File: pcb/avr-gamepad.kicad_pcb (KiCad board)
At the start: 2 copper layers, 53.1 x 53 mm, 56 parts, among them J1 Conn_01x06, J2 Conn_01x06, J3 Conn_01x05, J4 Conn_01x05, P1 USB_C_Plug_USB2.0, SW1 RESET, SW10 R2, SW11 A, SW13 Left, SW14 L2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

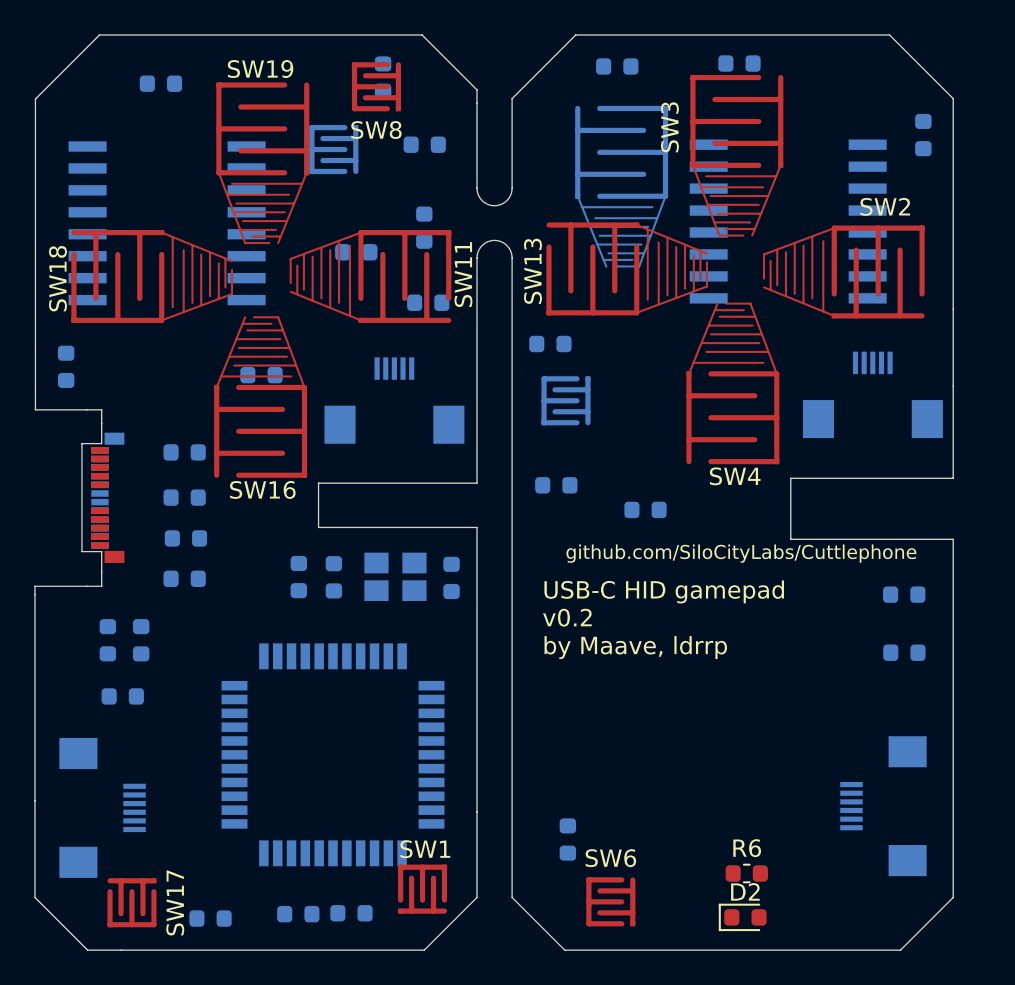
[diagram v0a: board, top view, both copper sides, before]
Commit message: change triggers to tact switches, add footprint
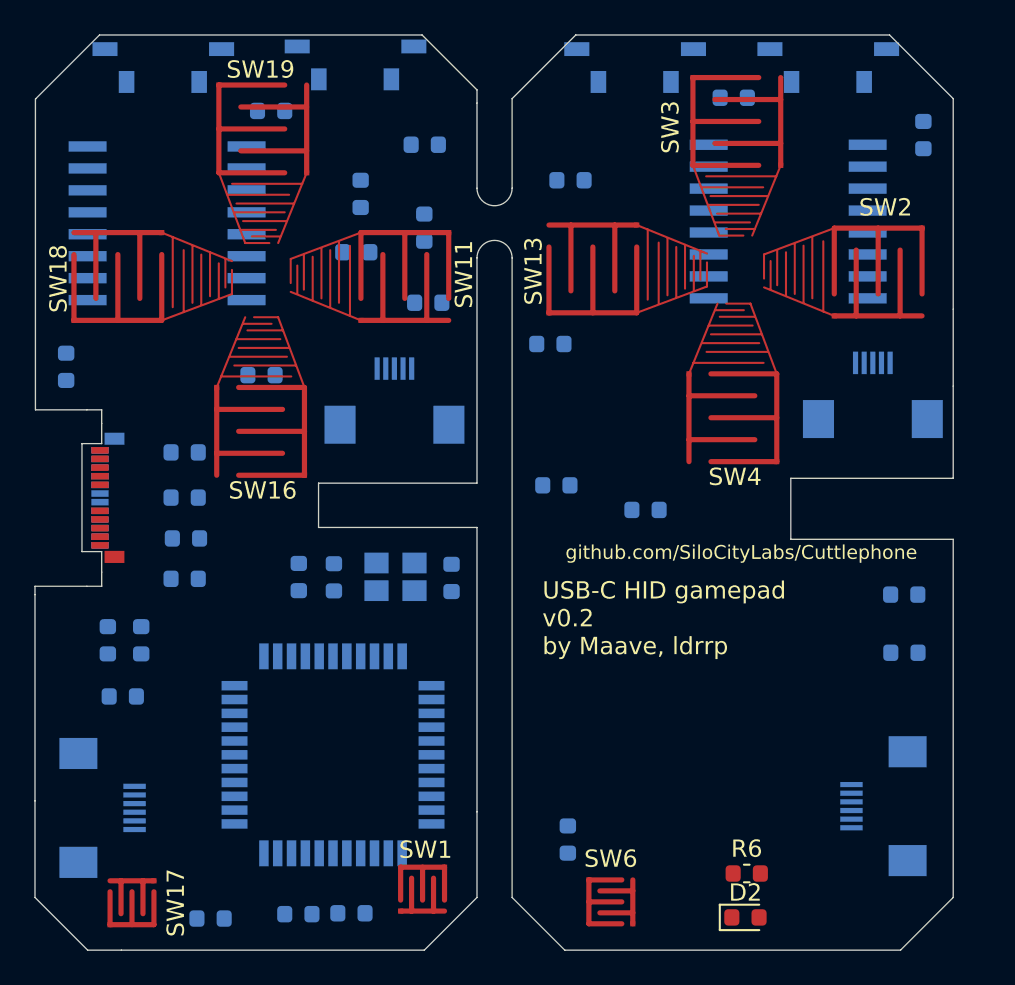
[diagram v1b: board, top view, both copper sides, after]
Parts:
- SW10, SW14: footprint button-contacts:Small -> right-angle-tact:TL3330
- SW7: footprint button-contacts:Large_tapered -> right-angle-tact:TL3330
- SW8: footprint button-contacts:Small -> right-angle-tact:TL3330; moved to B.Cu
- moved SW14 24.6 mm to (173.3, 82.2)
- moved SW10 11.0 mm to (134.9, 82.2)
- moved D4 7.12 mm to (158.4, 88.8), turned to 180 degrees
- moved D12 6.85 mm to (146.3, 89.6)
- moved D17 6.57 mm to (141.1, 84.8)
- moved SW7 5.03 mm to (162.2, 82.2), turned to 0 degrees
- moved D8 2.01 mm to (167.9, 84.0)
- moved SW8 1.82 mm to (146.0, 82.1)

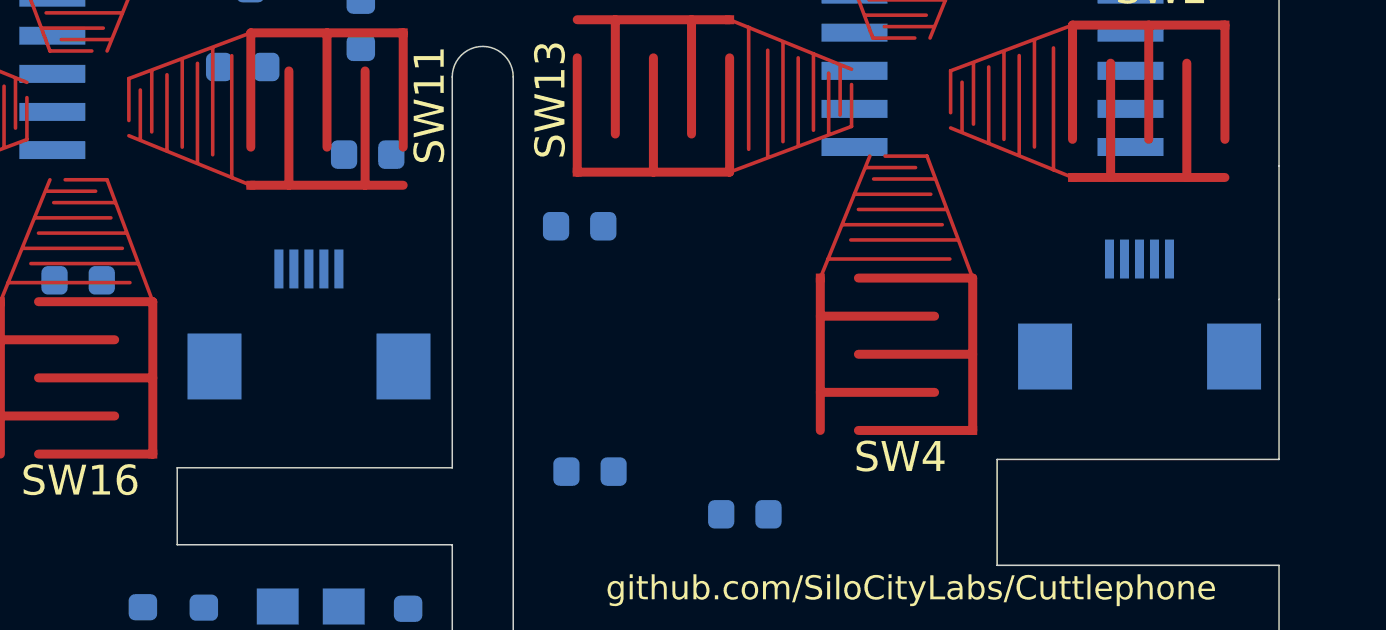
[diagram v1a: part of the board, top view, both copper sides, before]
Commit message: change 5-pin ffc to molex
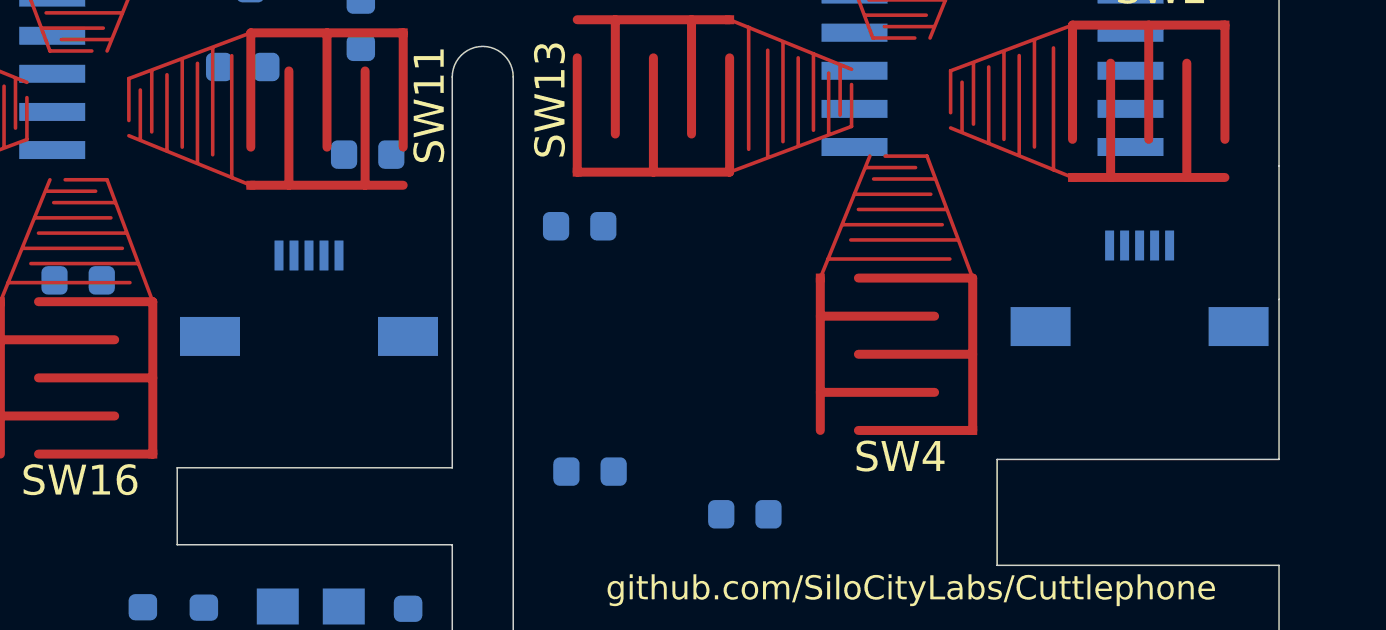
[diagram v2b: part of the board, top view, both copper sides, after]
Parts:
- J3, J4: footprint uxcell-ffc:uxcell_ffc_0.5pitch_1x05 -> molex_5051100592:5051100592

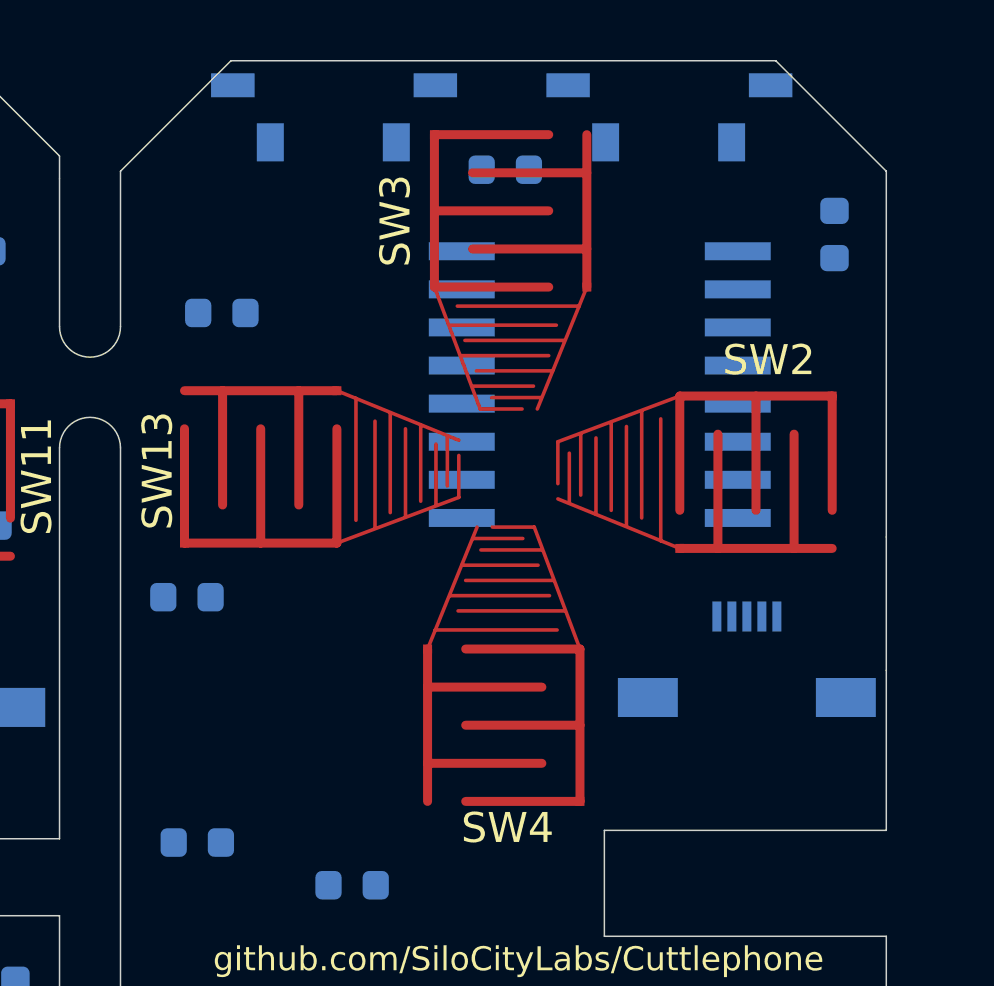
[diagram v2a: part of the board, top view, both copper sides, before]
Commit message: improve d-pad contacts
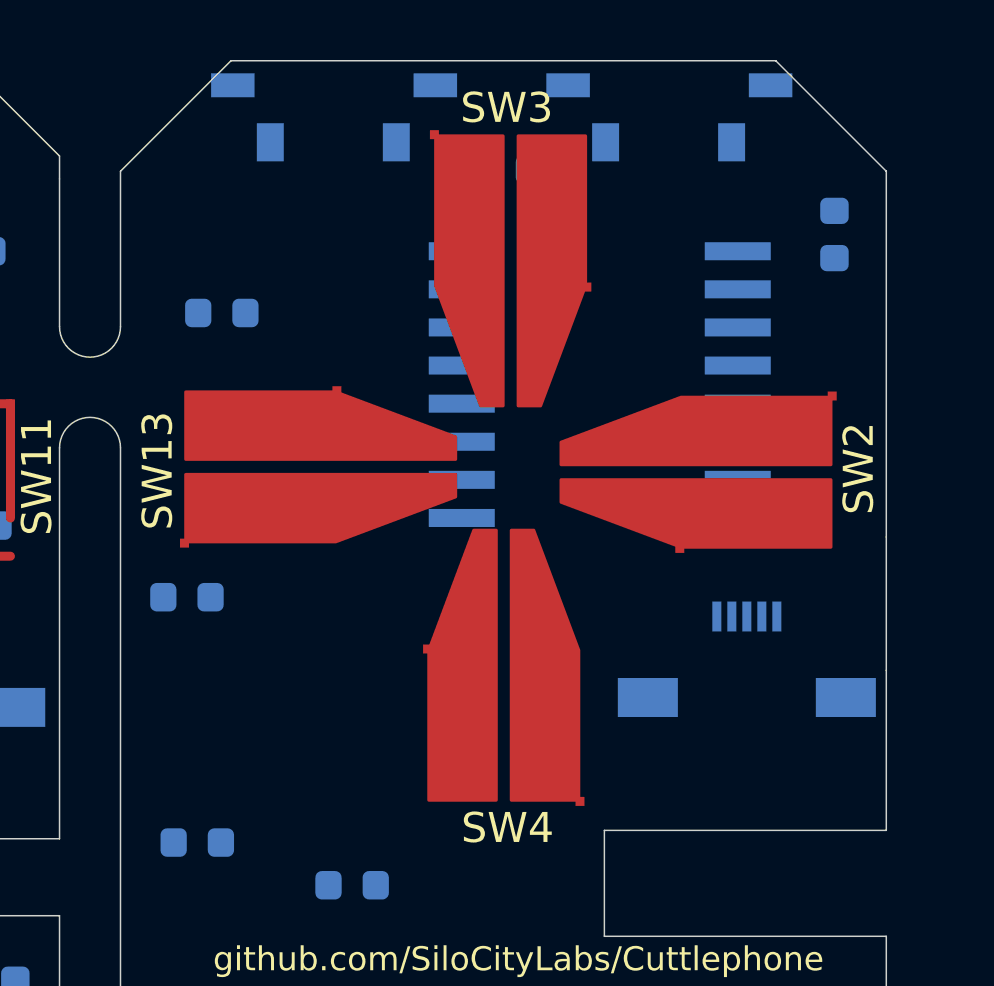
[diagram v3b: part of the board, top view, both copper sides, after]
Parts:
- SW13, SW2, SW3, SW4: footprint button-contacts:Large_tapered -> button-contacts:Dpad_Large_tapered

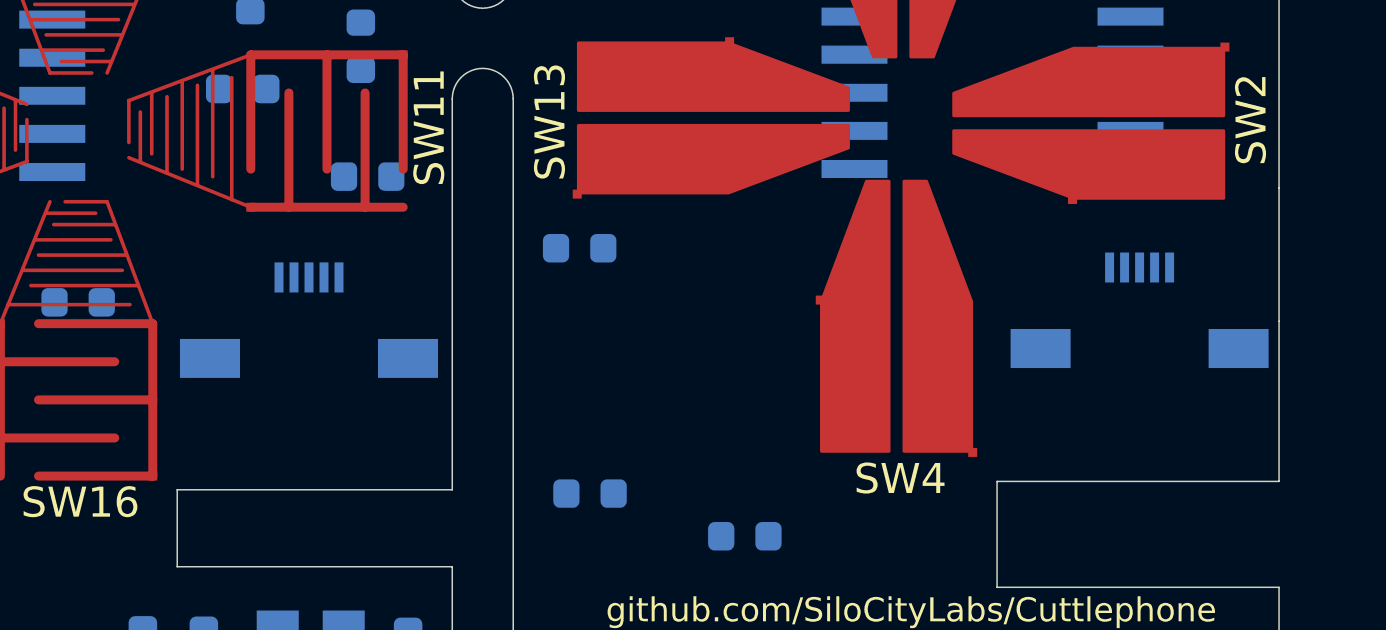
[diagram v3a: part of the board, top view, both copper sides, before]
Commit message: fix geometry calculations with BOSL shapes, add 1x04 FFC, experimental trigger
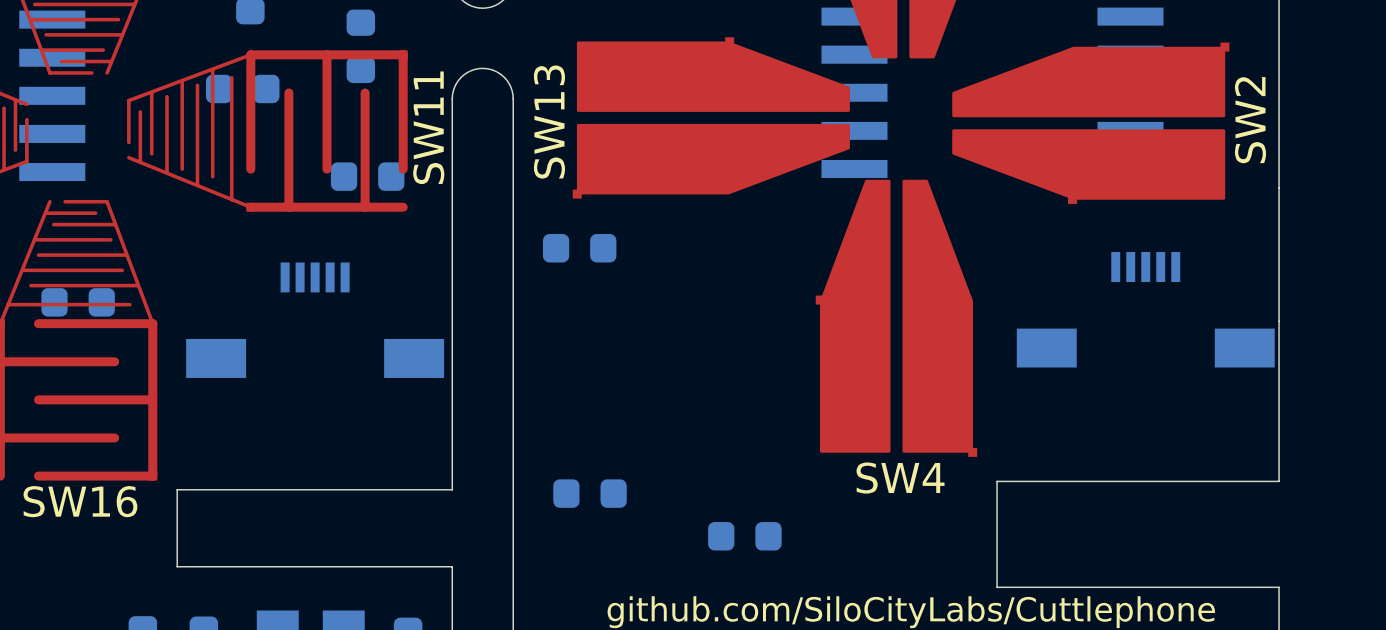
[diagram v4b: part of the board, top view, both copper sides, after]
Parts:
- moved J4 0.21 mm to (176.2, 101.2)
- moved J3 0.20 mm to (148.5, 101.5)
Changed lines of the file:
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@@
   )
   (module molex_5051100592:5051100592 (layer B.Cu)
-    (at 175.946 101.216 180)
+    (at 176.151 101.2 180)
     (descr 5051100592-3)
     (tags Connector)
@@
   )
   (module molex_5051100592:5051100592 (layer B.Cu)
-    (at 148.2594 101.5462 180)
+    (at 148.463 101.5462 180)
     (descr 5051100592-3)
     (tags Connector)

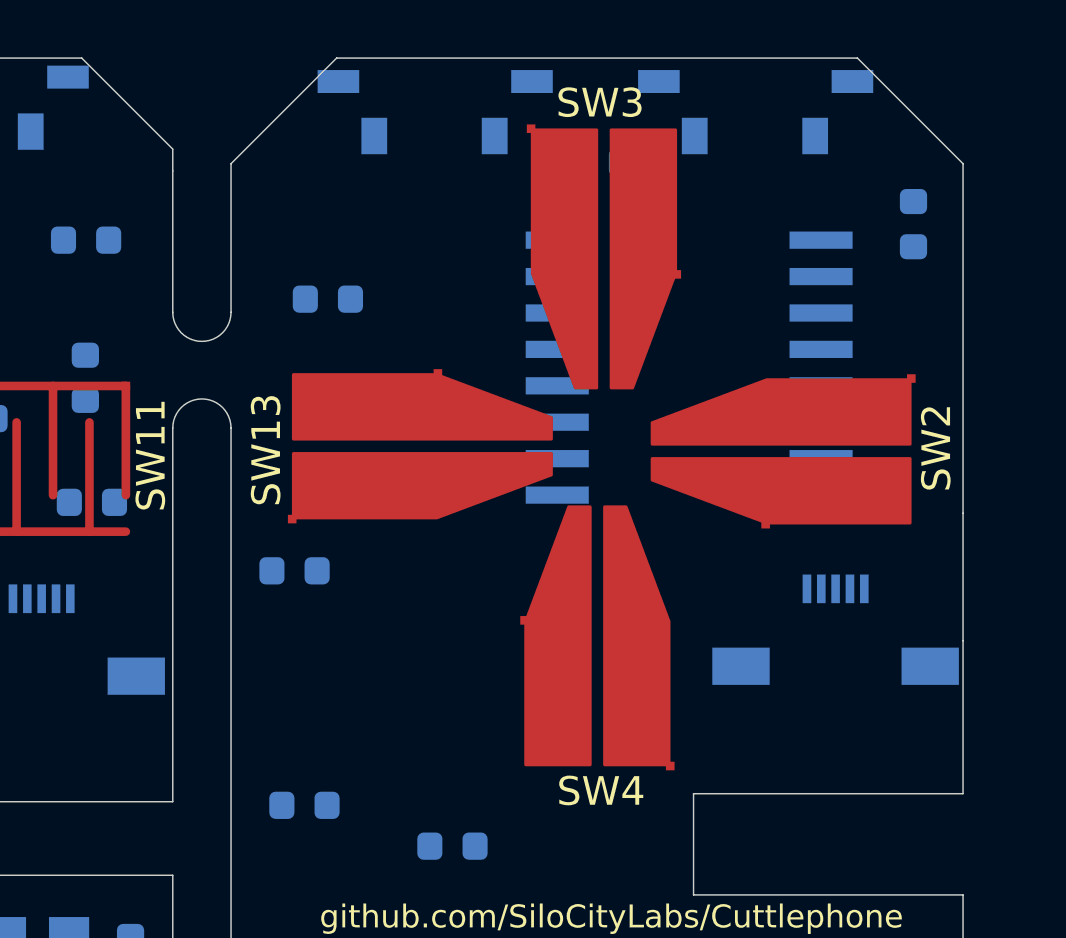
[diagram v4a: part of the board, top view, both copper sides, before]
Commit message: upgrade KiCad 6.0
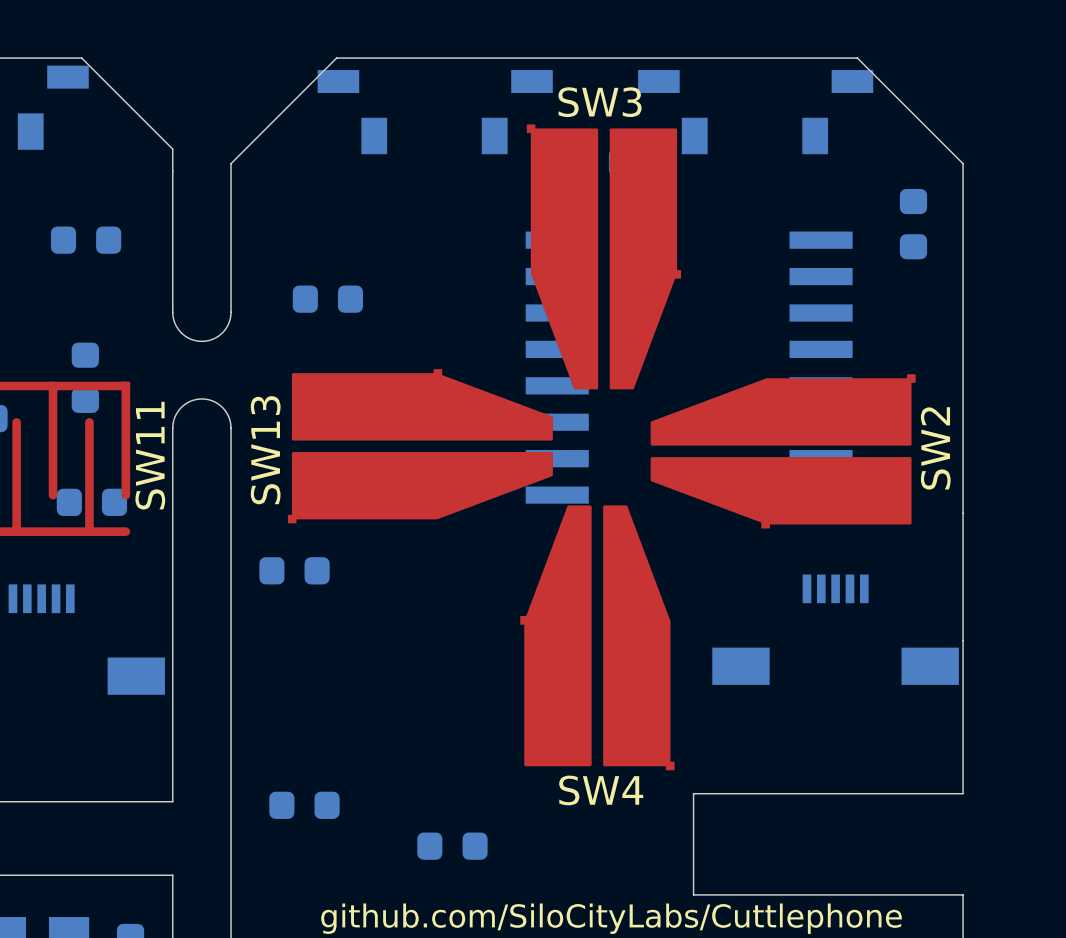
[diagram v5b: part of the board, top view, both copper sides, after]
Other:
- net class Default removed
- net class Power removed
